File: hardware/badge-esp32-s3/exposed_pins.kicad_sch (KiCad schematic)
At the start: 16 parts, among them CN1 B4B-PH-SM4-TB (LF)(SN), U10 FH2.54-09-02PZD, U11 FH2.54-09-04PZD, U12 FH2.54-09-03PZD, U13 FH2.54-09-02PZD, U14 FH2.54-09-04PZD, U15 FH2.54-09-04PZD, U16 FH2.54-09-04PZD, U19 FH2.54-09-02PZD, U6 ZX-SH1.0-4PWT, U7 FH2.54-09-02PZD, U8 FH2.54-09-03PZD, U9 FH2.54-09-03PZD

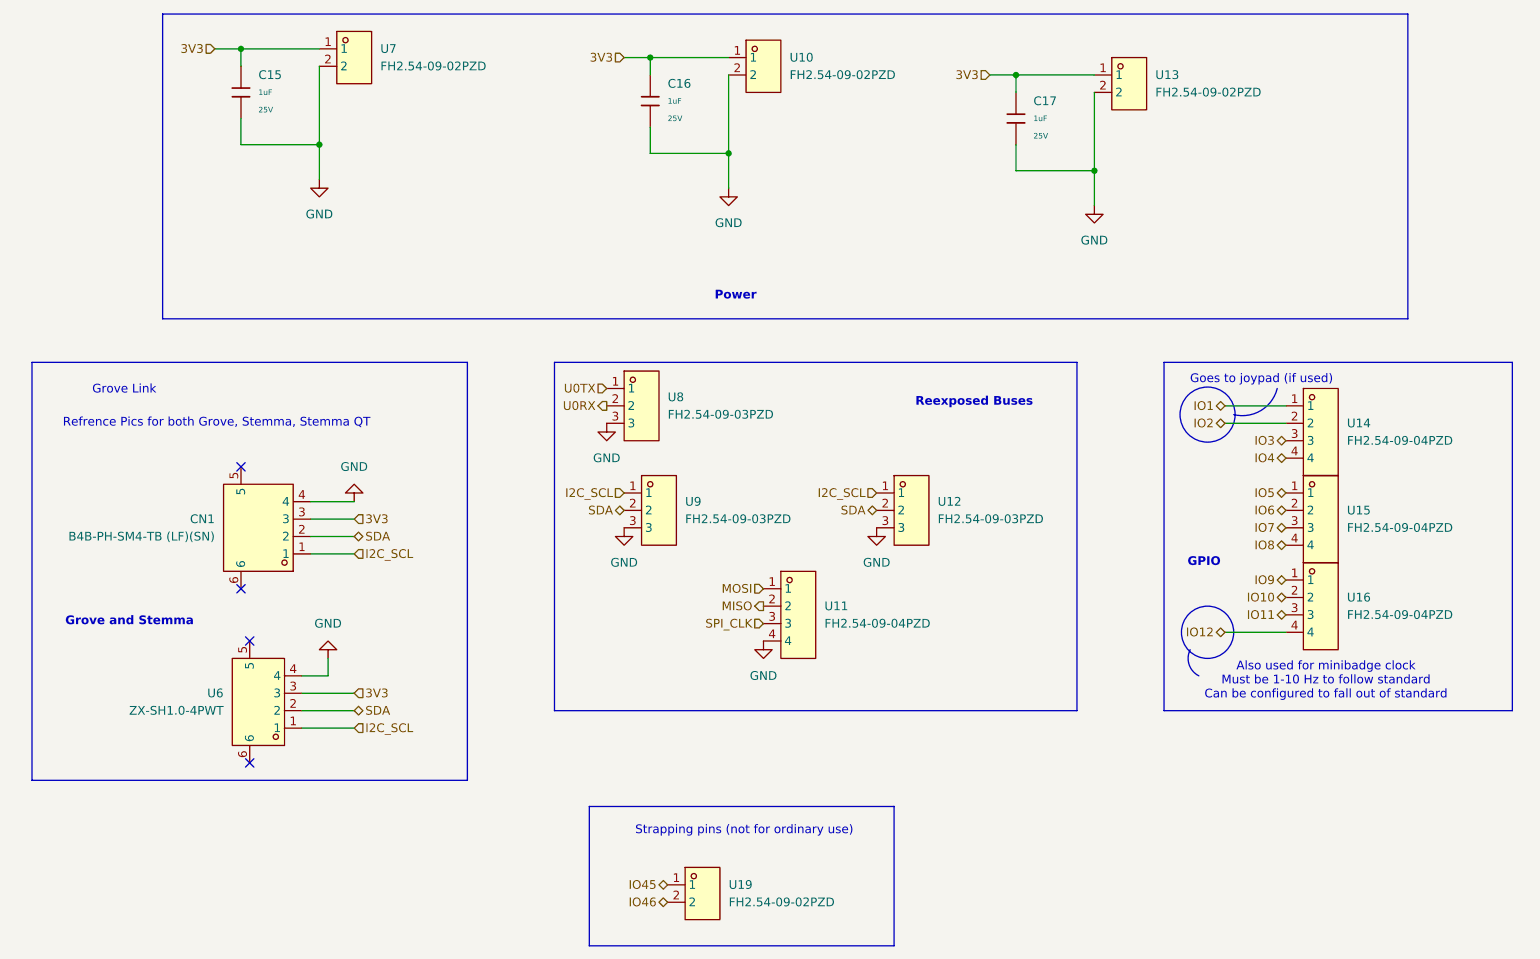
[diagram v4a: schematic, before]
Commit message: Consolidated the GPIO pins, communication pins, and power pins.
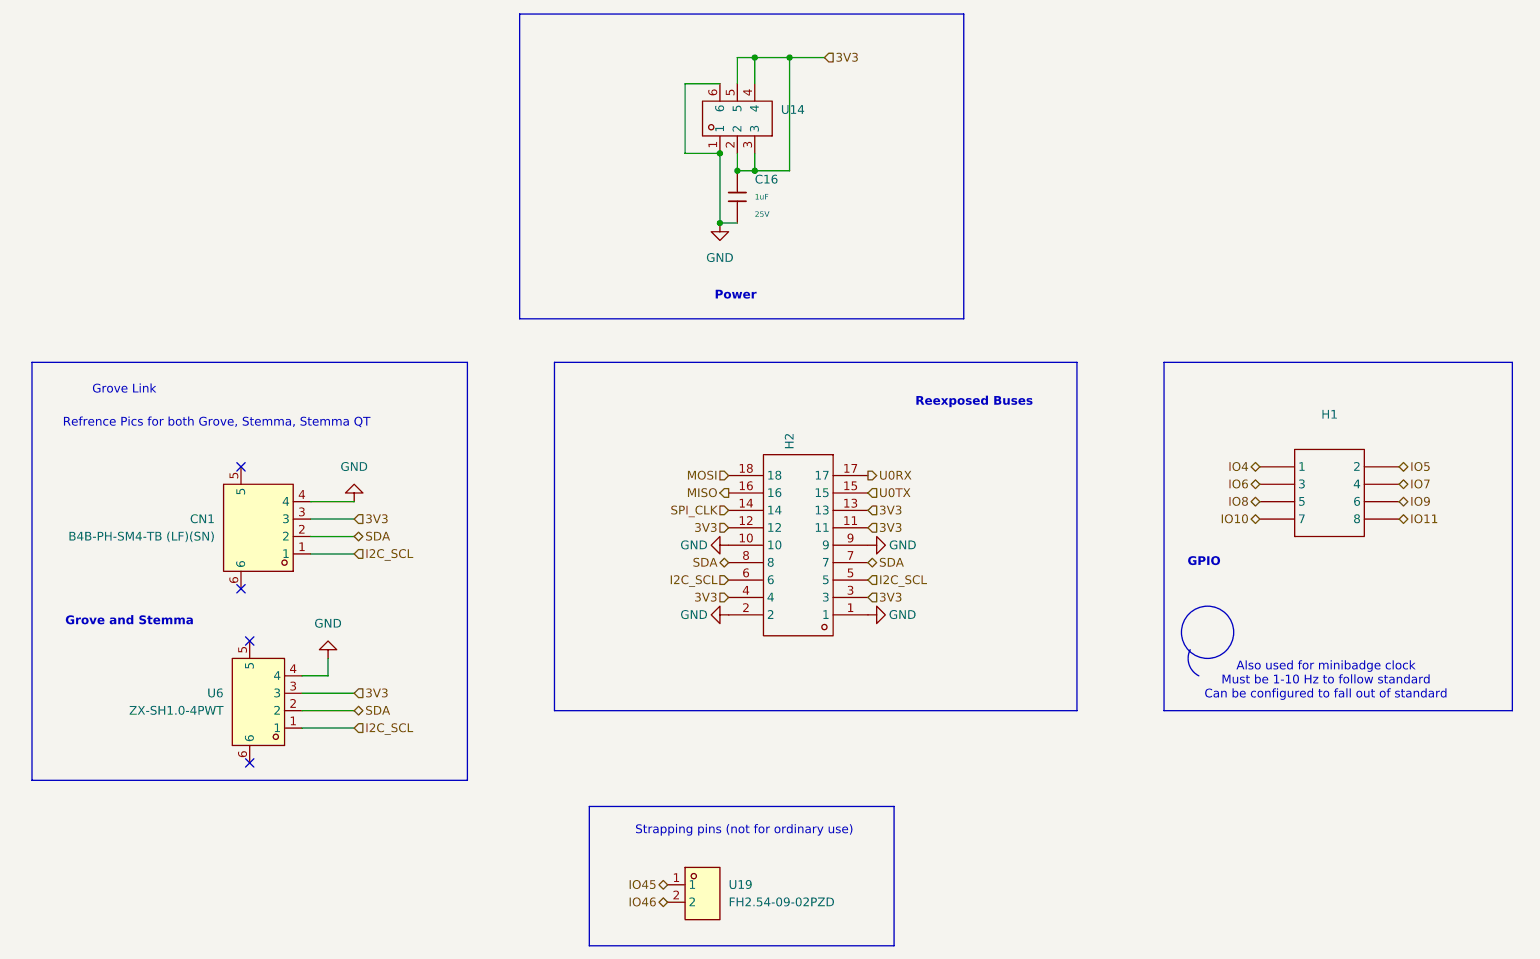
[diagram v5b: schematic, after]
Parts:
- removed C15, C17: 1uF, PCM_JLCPCB:C_0402, symbol PCM_JLCPCB-Capacitors:0402,1uF
- removed U10, U13, U7: FH2.54-09-02PZD, lcsc-lib:HDR-TH_2P-P2.54-V-M-5, symbol lcsc-lib:FH2.54-09-02PZD
- removed U11, U14, U15, U16: FH2.54-09-04PZD, lcsc-lib:HDR-TH_4P-P2.54-V-F, symbol lcsc-lib:FH2.54-09-04PZD
- removed U12, U8, U9: FH2.54-09-03PZD, lcsc-lib:HDR-TH_3P-P2.54-V-F, symbol lcsc-lib:FH2.54-09-03PZD
- added H1: ~, lcsc-lib:HDR-TH_8P-P2.54-V-F-R2-C4-S2.54, symbol lcsc-lib:DS1023-2*4SF11
- added H2: ~, lcsc-lib:HDR-TH_18P-P2.54-V-F-R2-C9-S2.54-1, symbol lcsc-lib:DS1023-2*9SF11
- added U14: ~, lcsc-lib:CONN-TH_HX-PM2.54-2X3P-ZC, symbol lcsc-lib:HX PM2.54-2X3P ZC
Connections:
- net 3V3: now also H2.11, H2.12, H2.13, H2.3, H2.4, U14.2, U14.3, U14.4, U14.5
- net GND: now also H2.1, H2.10, H2.2, H2.9, U14.1, U14.6
- net I2C_SCL: now also H2.5, H2.6
- net IO10: now also H1.7
- net IO11: now also H1.8
- net IO4: now also H1.1
- net IO5: now also H1.2
- net IO6: now also H1.3
- net IO7: now also H1.4
- net IO8: now also H1.5
- net IO9: now also H1.6
- net MISO: now also H2.16
- net MOSI: now also H2.18
- net SDA: now also H2.7, H2.8
- net SPI_CLK: now also H2.14
- net U0RX: now also H2.17
- net U0TX: now also H2.15
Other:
- note removed: "Goes to joypad (if used)"
- moved on the sheet: C16

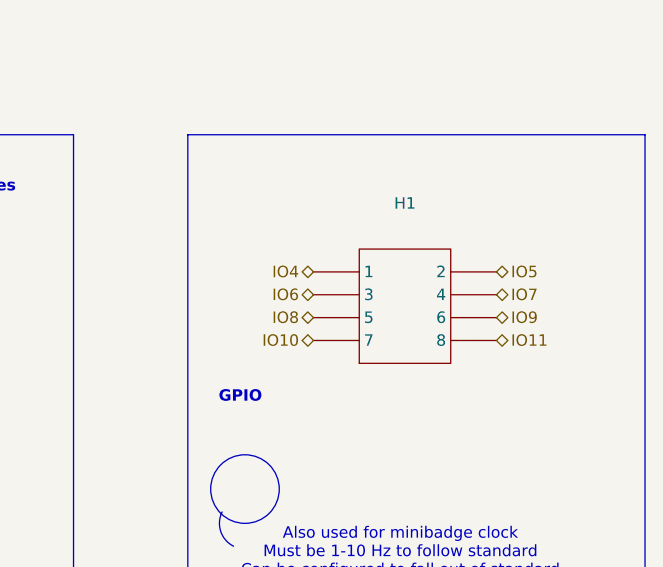
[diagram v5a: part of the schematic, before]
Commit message: Swapped the RGB led pins.
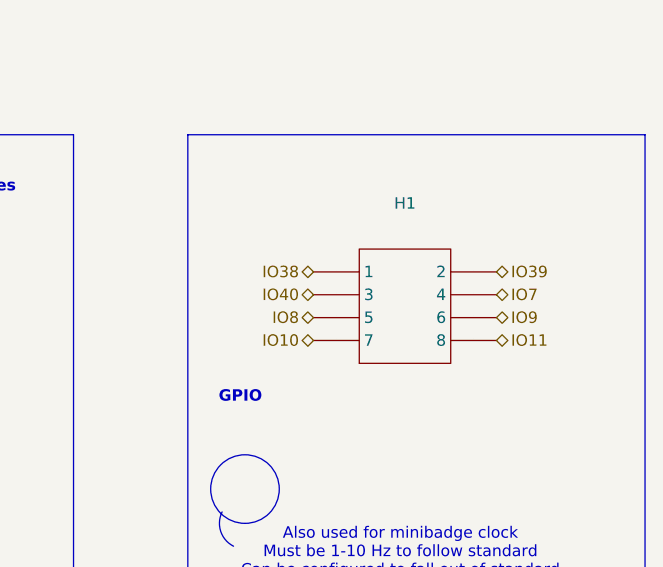
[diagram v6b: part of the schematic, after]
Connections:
- net IO4 renamed IO38
- net IO5 renamed IO39
- net IO6 renamed IO40
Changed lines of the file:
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@@
 		)
 	)
-	(hierarchical_label "IO5"
+	(hierarchical_label "IO39"
 		(shape bidirectional)
 		(at 237.49 91.44 0)
@@
 		)
 	)
-	(hierarchical_label "IO6"
+	(hierarchical_label "IO40"
 		(shape bidirectional)
 		(at 217.17 93.98 180)
@@
 		)
 	)
-	(hierarchical_label "IO4"
+	(hierarchical_label "IO38"
 		(shape bidirectional)
 		(at 217.17 91.44 180)

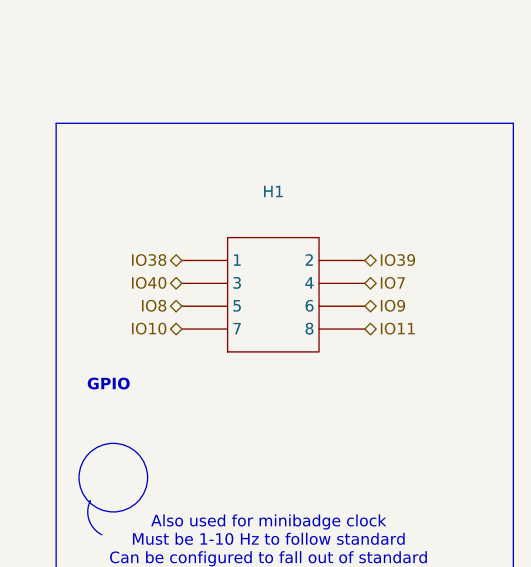
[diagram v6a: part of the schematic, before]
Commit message: Updated the buzzer to not use a jtag pin.
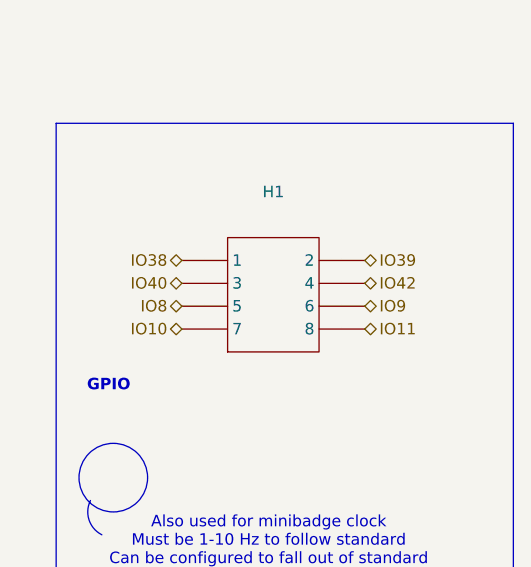
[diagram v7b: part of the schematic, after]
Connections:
- net IO7 renamed IO42
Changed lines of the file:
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@@
 		)
 	)
-	(hierarchical_label "IO7"
+	(hierarchical_label "IO42"
 		(shape bidirectional)
 		(at 237.49 93.98 0)

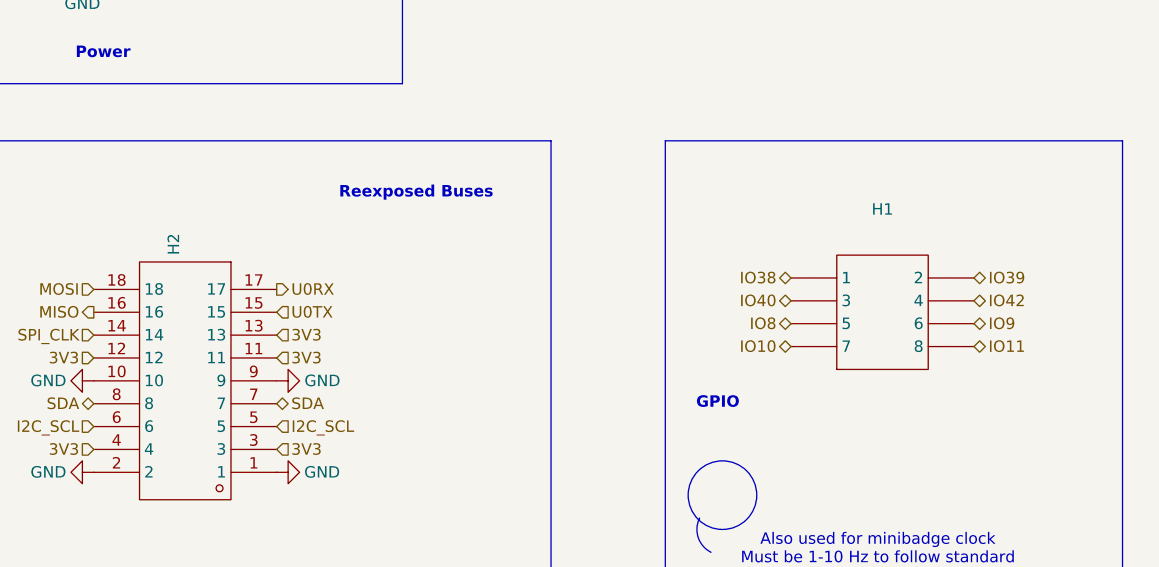
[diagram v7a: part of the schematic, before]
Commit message: Updated the exposed gpio block.
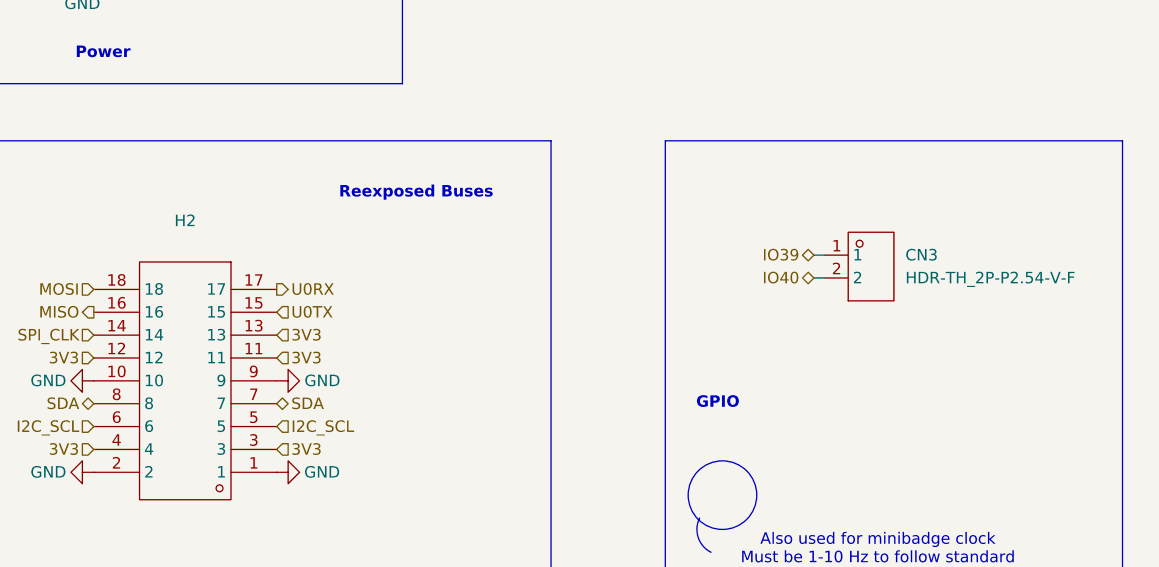
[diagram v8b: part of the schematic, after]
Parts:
- removed H1: ~, lcsc-lib:HDR-TH_8P-P2.54-V-F-R2-C4-S2.54, symbol lcsc-lib:DS1023-2*4SF11
- added CN3: HDR-TH_2P-P2.54-V-F, lcsc-lib:HDR-TH_2P-P2.54-V-F, symbol lcsc-lib:HX PM2.54-1X2P ZC-Y
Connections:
- net IO39: now also CN3.1
- net IO40: now also CN3.2
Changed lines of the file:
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@@
+	(wire
+		(pts
+			(xy 219.71 88.9) (xy 220.98 88.9)
+		)
+		(stroke
+			(width 0)
+			(type default)
+		)
+	)
 	(wire
 		(pts
 			(xy 133.35 45.72) (xy 138.43 45.72)
+		)
+		(stroke
+			(width 0)
+			(type default)
+		)
+	)
+	(wire
+		(pts
+			(xy 219.71 91.44) (xy 220.98 91.44)
 		)
 		(stroke
@@
 		)
 	)
-	(hierarchical_label "IO11"
-		(shape bidirectional)
-		(at 237.49 99.06 0)
-		(effects
-			(font
-				(size 1.27 1.27)
-			)
-			(justify left)
-		)
-	)
 	(hierarchical_label "SDA"
 		(shape bidirectional)
@@
 		)
 	)
-	(hierarchical_label "IO9"
-		(shape bidirectional)
-		(at 237.49 96.52 0)
-		(effects
-			(font
-				(size 1.27 1.27)
-			)
-			(justify left)
-		)
-	)
 	(hierarchical_label "SDA"
 		(shape bidirectional)
@@
 	(hierarchical_label "IO39"
 		(shape bidirectional)
-		(at 237.49 91.44 0)
-		(effects
-			(font
-				(size 1.27 1.27)
-			)
-			(justify left)
+		(at 219.71 88.9 180)
+		(effects
+			(font
+				(size 1.27 1.27)
+			)
+			(justify right)
 		)
 	)
@@
 		)
 	)
-	(hierarchical_label "IO42"
-		(shape bidirectional)
-		(at 237.49 93.98 0)
-		(effects
-			(font
-				(size 1.27 1.27)
-			)
-			(justify left)
-		)
-	)
 	(hierarchical_label "3V3"
 		(shape input)
@@
 		)
 	)
-	(hierarchical_label "IO10"
-		(shape bidirectional)
-		(at 217.17 99.06 180)
-		(effects
-			(font
-				(size 1.27 1.27)
-			)
-			(justify right)
-		)
-	)
-	(hierarchical_label "IO40"
-		(shape bidirectional)
-		(at 217.17 93.98 180)
-		(effects
-			(font
-				(size 1.27 1.27)
-			)
-			(justify right)
-		)
-	)
-	(hierarchical_label "IO8"
-		(shape bidirectional)
-		(at 217.17 96.52 180)
-		(effects
-			(font
-				(size 1.27 1.27)
-			)
-			(justify right)
-		)
-	)
 	(hierarchical_label "3V3"
 		(shape input)
@@
 		)
 	)
-	(hierarchical_label "IO38"
+	(hierarchical_label "IO40"
 		(shape bidirectional)
-		(at 217.17 91.44 180)
+		(at 219.71 91.44 180)
 		(effects
 			(font
@@
 				(path "/e2af9a6c-dbe9-4de2-9ba6-ea213a7300ec/069334c8-a377-4249-b519-18db4f2b1959"
 					(reference "#PWR049")
+					(unit 1)
+				)
+			)
+		)
+	)
+	(symbol
+		(lib_id "lcsc-lib:HX PM2.54-1X2P ZC-Y")
+		(at 226.06 90.17 0)
+		(unit 1)
+		(exclude_from_sim no)
+		(in_bom yes)
+		(on_board yes)
+		(dnp no)
+		(fields_autoplaced yes)
+		(property "Reference" "CN3"
+			(at 229.87 88.8999 0)
+			(effects
+				(font
+					(size 1.27 1.27)
+				)
+				(justify left)
+			)
+		)
+		(property "Value" "HDR-TH_2P-P2.54-V-F"
+			(at 229.87 91.4399 0)
+			(effects
+				(font
+					(size 1.27 1.27)
+				)
+				(justify left)
+			)
+		)
+		(property "Footprint" "lcsc-lib:HDR-TH_2P-P2.54-V-F"
+			(at 226.06 90.17 0)
+			(effects
+				(font
+					(size 1.27 1.27)
+				)
+				(hide yes)
+			)
+		)
+		(property "Datasheet" "https://item.szlcsc.com/datasheet/HX%2520PM2.54-1x2P%2520ZC-Y/24075299.html"
+			(at 226.06 90.17 0)
+			(effects
+				(font
+					(size 1.27 1.27)
+				)
+				(hide yes)
+			)
+		)
+		(property "Description" "Holes Structure:1x2P Pitch:2.54mm Row Spacing:- Circular Hole / Square Hole:Square Hole Mounting Type:Through Hole Number of Rows:1 Number of Positions:2P Current Rating:3A Voltage Rating (Max):1kV Holes Direction:Top Insulation Height:8.5mm Contact Mater"
+			(at 226.06 90.17 0)
+			(effects
+				(font
+					(size 1.27 1.27)
+				)
+				(hide yes)
+			)
+		)
+		(property "Manufacturer Part" "HX PM2.54-1x2P ZC-Y"
+			(at 226.06 90.17 0)
+			(effects
+				(font
+					(size 1.27 1.27)
+				)
+				(hide yes)
+			)
+		)
+		(property "Manufacturer" "hanxia(韩下)"
+			(at 226.06 90.17 0)
+			(effects
+				(font
+					(size 1.27 1.27)
+				)
+				(hide yes)
+			)
+		)
+		(property "Supplier Part" "C22438152"
+			(at 226.06 90.17 0)
+			(effects
+				(font
+					(size 1.27 1.27)
+				)
+				(hide yes)
+			)
+		)
+		(property "Supplier" "LCSC"
+			(at 226.06 90.17 0)
+			(effects
+				(font
+					(size 1.27 1.27)
+				)
+				(hide yes)
+			)
+		)
+		(property "LCSC Part Name" "1x2P 间距:2.54mm 直插"
+			(at 226.06 90.17 0)
+			(effects
+				(font
+					(size 1.27 1.27)
+				)
+				(hide yes)
+			)
+		)
+		(pin "2"
+		)
+		(pin "1"
+		)
+		(instances
+			(project ""
+				(path "/e2af9a6c-dbe9-4de2-9ba6-ea213a7300ec/069334c8-a377-4249-b519-18db4f2b1959"
+					(reference "CN3")
 					(unit 1)
 				)
@@
 		(fields_autoplaced yes)
 		(property "Reference" "H2"
-			(at 148.5899 88.9 90)
-			(effects
-				(font
-					(size 1.27 1.27)
-				)
-				(justify right)
+			(at 149.86 85.09 0)
+			(effects
+				(font
+					(size 1.27 1.27)
+				)
 			)
 		)
 		(property "Value" "~"
-			(at 151.1299 88.9 90)
-			(effects
-				(font
-					(size 1.27 1.27)
-				)
-				(justify right)
+			(at 149.86 87.63 0)
+			(effects
+				(font
+					(size 1.27 1.27)
+				)
 			)
 		)
@@
 					(unit 1)
 				)
-			)
-		)
-	)
-	(symbol
-		(lib_id "lcsc-lib:DS1023-2*4SF11")
-		(at 227.33 95.25 0)
-		(unit 1)
-		(exclude_from_sim no)
-		(in_bom yes)
-		(on_board yes)
-		(dnp no)
-		(fields_autoplaced yes)
-		(property "Reference" "H1"
-			(at 227.33 83.82 0)
-			(effects
-				(font
-					(size 1.27 1.27)
-				)
-			)
-		)
-		(property "Value" "~"
-			(at 227.33 86.36 0)
-			(effects
-				(font
-					(size 1.27 1.27)
-				)
-			)
-		)
-		(property "Footprint" "lcsc-lib:HDR-TH_8P-P2.54-V-F-R2-C4-S2.54"
-			(at 227.33 95.25 0)
-			(effects
-				(font
-					(size 1.27 1.27)
-				)
-				(hide yes)
-			)
-		)
-		(property "Datasheet" "https://item.szlcsc.com/datasheet/DS1023-2*4SF11/93464.html"
-			(at 227.33 95.25 0)
-			(effects
-				(font
-					(size 1.27 1.27)
-				)
-				(hide yes)
-			)
-		)
-		(property "Description" "Holes Structure:2x4P Pitch:2.54mm Row Spacing:2.54mm Mounting Type:Through Hole Number of Rows:2 Number of Positions:8P Current Rating:3A Voltage Rating (Max):600V Holes Direction:Top Insulation Height:8.5mm Contact Material:- Contact Plating:Gold Operati"
-			(at 227.33 95.25 0)
-			(effects
-				(font
-					(size 1.27 1.27)
-				)
-				(hide yes)
-			)
-		)
-		(property "Manufacturer Part" "DS1023-2*4SF11"
-			(at 227.33 95.25 0)
-			(effects
-				(font
-					(size 1.27 1.27)
-				)
-				(hide yes)
-			)
-		)
-		(property "Manufacturer" "CONNFLY"
-			(at 227.33 95.25 0)
-			(effects
-				(font
-					(size 1.27 1.27)
-				)
-				(hide yes)
-			)
-		)
-		(property "Supplier Part" "C92271"
-			(at 227.33 95.25 0)
-			(effects
-				(font
-					(size 1.27 1.27)
-				)
-				(hide yes)
-			)
-		)
-		(property "Supplier" "LCSC"
-			(at 227.33 95.25 0)
-			(effects
-				(font
-					(size 1.27 1.27)
-				)
-				(hide yes)
-			)
-		)
-		(property "LCSC Part Name" "黑色 2x4P 间距:2.54mm 直插"
-			(at 227.33 95.25 0)
-			(effects
-				(font
-					(size 1.27 1.27)
-				)
-				(hide yes)
-			)
-		)
-		(pin "6"
-		)
-		(pin "8"
-		)
-		(pin "4"
-		)
-		(pin "1"
-		)
-		(pin "3"
-		)
-		(pin "5"
-		)
-		(pin "7"
-		)
-		(pin "2"
-		)
-		(instances
-			(project ""
-				(path "/e2af9a6c-dbe9-4de2-9ba6-ea213a7300ec/069334c8-a377-4249-b519-18db4f2b1959"
-					(reference "H1")
-					(unit 1)
-				)
